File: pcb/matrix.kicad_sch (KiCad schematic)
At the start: 179 parts, among them SW10 Tab, SW11 CapsLock, SW12 Shift, SW13 Ctrl, SW14 F1, SW15 1, SW16 Q, SW17 A, SW18 Z, SW19 Win, SW20 F2, SW21 2, SW22 W, SW23 S, SW24 X, SW25 F3, SW26 3, SW27 E, SW28 D, SW29 C, SW30 F4, SW31 4, SW32 R, SW33 F, SW34 V, SW35 F5, SW36 5, SW37 T, SW38 G, SW39 B, SW4 M1, SW40 Space, SW41 F6, SW42 6, SW43 Y, SW44 H, SW45 N, SW46 F7, SW47 7, SW48 U, SW49 J, SW5 M2, SW50 M, SW51 F8, SW52 8, SW53 I, SW54 K, SW55 Comma, SW56 RAlt, SW57 F9, SW58 9, SW59 O, SW6 M3, SW60 L, SW61 Period, SW62 RFn, SW63 F10, SW64 0, SW65 P, SW66 Semicolon, SW67 Slash, SW68 RCtrl, SW69 F11, SW7 M4, SW70 Minus, SW71 LBrkt, SW72 Quote, SW73 RShift, SW74 F12, SW75 Equals, SW76 RBrkt, SW77 Enter, SW78 LArr, SW79 F13, SW8 Esc, SW80 Bksp, SW81 Bkslash, SW82 UArr, SW83 DArr, SW84 Knob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

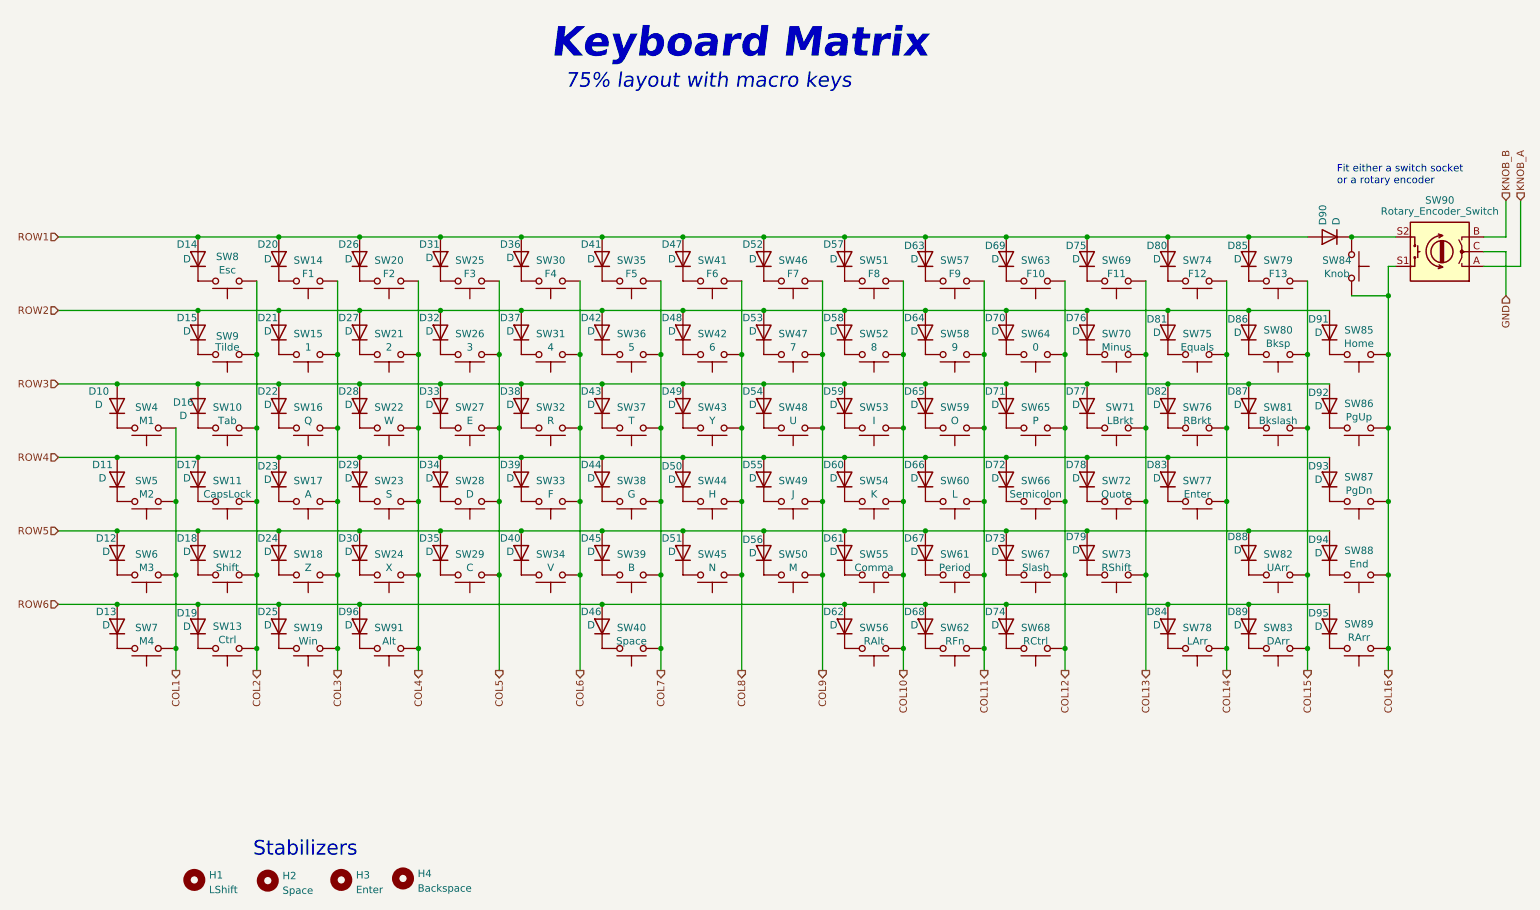
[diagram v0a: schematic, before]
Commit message: Change value fields for socket assembly
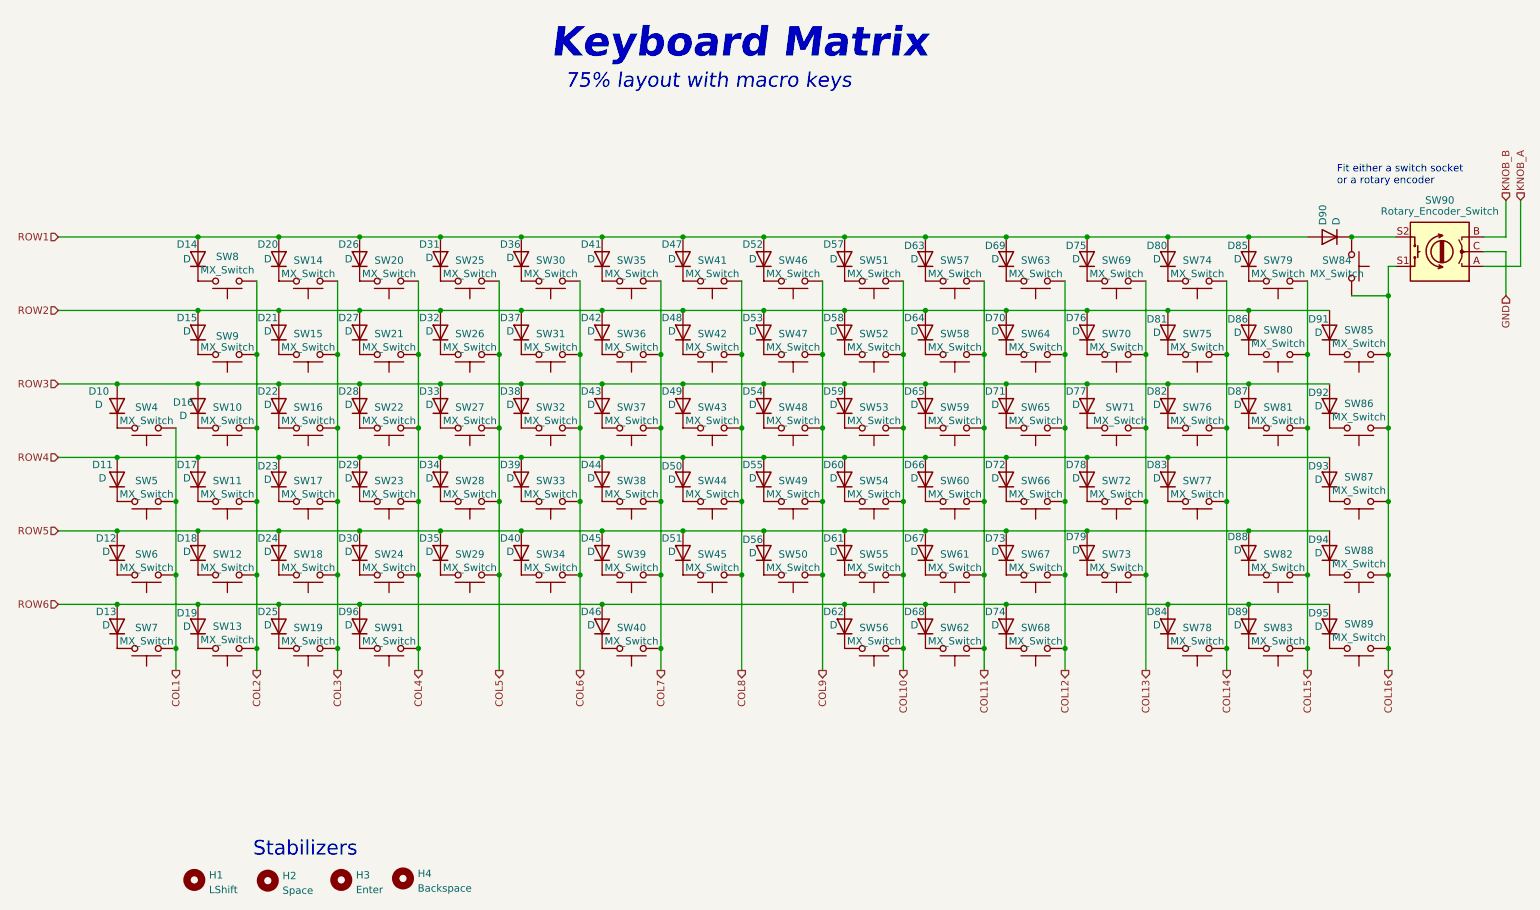
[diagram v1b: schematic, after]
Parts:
- SW10: value Tab -> MX_Switch; LSCS (none) -> C5156480
- SW11: value CapsLock -> MX_Switch; LSCS (none) -> C5156480
- SW12: value Shift -> MX_Switch; LSCS (none) -> C5156480
- SW13: value Ctrl -> MX_Switch; LSCS (none) -> C5156480
- SW14: value F1 -> MX_Switch; LSCS (none) -> C5156480
- SW15: value 1 -> MX_Switch; LSCS (none) -> C5156480
- SW16: value Q -> MX_Switch; LSCS (none) -> C5156480
- SW17: value A -> MX_Switch; LSCS (none) -> C5156480
- SW18: value Z -> MX_Switch; LSCS (none) -> C5156480
- SW19: value Win -> MX_Switch; LSCS (none) -> C5156480
- SW20: value F2 -> MX_Switch; LSCS (none) -> C5156480
- SW21: value 2 -> MX_Switch; LSCS (none) -> C5156480
- SW22: value W -> MX_Switch; LSCS (none) -> C5156480
- SW23: value S -> MX_Switch; LSCS (none) -> C5156480
- SW24: value X -> MX_Switch; LSCS (none) -> C5156480
- SW25: value F3 -> MX_Switch; LSCS (none) -> C5156480
- SW26: value 3 -> MX_Switch; LSCS (none) -> C5156480
- SW27: value E -> MX_Switch; LSCS (none) -> C5156480
- SW28: value D -> MX_Switch; LSCS (none) -> C5156480
- SW29: value C -> MX_Switch; LSCS (none) -> C5156480
- SW30: value F4 -> MX_Switch; LSCS (none) -> C5156480
- SW31: value 4 -> MX_Switch; LSCS (none) -> C5156480
- SW32: value R -> MX_Switch; LSCS (none) -> C5156480
- SW33: value F -> MX_Switch; LSCS (none) -> C5156480
- SW34: value V -> MX_Switch; LSCS (none) -> C5156480
- SW35: value F5 -> MX_Switch; LSCS (none) -> C5156480
- SW36: value 5 -> MX_Switch; LSCS (none) -> C5156480
- SW37: value T -> MX_Switch; LSCS (none) -> C5156480
- SW38: value G -> MX_Switch; LSCS (none) -> C5156480
- SW39: value B -> MX_Switch; LSCS (none) -> C5156480
- SW4: value M1 -> MX_Switch; LSCS (none) -> C5156480
- SW40: value Space -> MX_Switch; LSCS (none) -> C5156480
- SW41: value F6 -> MX_Switch; LSCS (none) -> C5156480
- SW42: value 6 -> MX_Switch; LSCS (none) -> C5156480
- SW43: value Y -> MX_Switch; LSCS (none) -> C5156480
- SW44: value H -> MX_Switch; LSCS (none) -> C5156480
- SW45: value N -> MX_Switch; LSCS (none) -> C5156480
- SW46: value F7 -> MX_Switch; LSCS (none) -> C5156480
- SW47: value 7 -> MX_Switch; LSCS (none) -> C5156480
- SW48: value U -> MX_Switch; LSCS (none) -> C5156480
- SW49: value J -> MX_Switch; LSCS (none) -> C5156480
- SW5: value M2 -> MX_Switch; LSCS (none) -> C5156480
- SW50: value M -> MX_Switch; LSCS (none) -> C5156480
- SW51: value F8 -> MX_Switch; LSCS (none) -> C5156480
- SW52: value 8 -> MX_Switch; LSCS (none) -> C5156480
- SW53: value I -> MX_Switch; LSCS (none) -> C5156480
- SW54: value K -> MX_Switch; LSCS (none) -> C5156480
- SW55: value Comma -> MX_Switch; LSCS (none) -> C5156480
- SW56: value RAlt -> MX_Switch; LSCS (none) -> C5156480
- SW57: value F9 -> MX_Switch; LSCS (none) -> C5156480
- SW58: value 9 -> MX_Switch; LSCS (none) -> C5156480
- SW59: value O -> MX_Switch; LSCS (none) -> C5156480
- SW6: value M3 -> MX_Switch; LSCS (none) -> C5156480
- SW60: value L -> MX_Switch; LSCS (none) -> C5156480
- SW61: value Period -> MX_Switch; LSCS (none) -> C5156480
- SW62: value RFn -> MX_Switch; LSCS (none) -> C5156480
- SW63: value F10 -> MX_Switch; LSCS (none) -> C5156480
- SW64: value 0 -> MX_Switch; LSCS (none) -> C5156480
- SW65: value P -> MX_Switch; LSCS (none) -> C5156480
- SW66: value Semicolon -> MX_Switch; LSCS (none) -> C5156480
- SW67: value Slash -> MX_Switch; LSCS (none) -> C5156480
- SW68: value RCtrl -> MX_Switch; LSCS (none) -> C5156480
- SW69: value F11 -> MX_Switch; LSCS (none) -> C5156480
- SW7: value M4 -> MX_Switch; LSCS (none) -> C5156480
- SW70: value Minus -> MX_Switch; LSCS (none) -> C5156480
- SW71: value LBrkt -> MX_Switch; LSCS (none) -> C5156480
- SW72: value Quote -> MX_Switch; LSCS (none) -> C5156480
- SW73: value RShift -> MX_Switch; LSCS (none) -> C5156480
- SW74: value F12 -> MX_Switch; LSCS (none) -> C5156480
- SW75: value Equals -> MX_Switch; LSCS (none) -> C5156480
- SW76: value RBrkt -> MX_Switch; LSCS (none) -> C5156480
- SW77: value Enter -> MX_Switch; LSCS (none) -> C5156480
- SW78: value LArr -> MX_Switch; LSCS (none) -> C5156480
- SW79: value F13 -> MX_Switch; LSCS (none) -> C5156480
- SW8: value Esc -> MX_Switch; LSCS (none) -> C5156480
- SW80: value Bksp -> MX_Switch; LSCS (none) -> C5156480
- SW81: value Bkslash -> MX_Switch; LSCS (none) -> C5156480
- SW82: value UArr -> MX_Switch; LSCS (none) -> C5156480
- SW83: value DArr -> MX_Switch; LSCS (none) -> C5156480
- SW84: value Knob -> MX_Switch; LSCS (none) -> C5156480
- SW85: value Home -> MX_Switch; LSCS (none) -> C5156480
- SW86: value PgUp -> MX_Switch; LSCS (none) -> C5156480
- SW87: value PgDn -> MX_Switch; LSCS (none) -> C5156480
- SW88: value End -> MX_Switch; LSCS (none) -> C5156480
- SW89: value RArr -> MX_Switch; LSCS (none) -> C5156480
- SW9: value Tilde -> MX_Switch; LSCS (none) -> C5156480
- SW91: value Alt -> MX_Switch; LSCS (none) -> C5156480

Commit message: Move SWD header, fix DRC issues
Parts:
- SW84: footprint Switch_Keyboard_Kailh:SW_Hotswap_Kailh_MX_plated_1.00u -> Switch_Keyboard_Kailh:SW_Hotswap_Kailh_MX_1.00u
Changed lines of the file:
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@@
     (property "Reference" "SW84" (id 0) (at 247.65 72.6186 90))
     (property "Value" "MX_Switch" (id 1) (at 247.65 74.93 90))
-    (property "Footprint" "Switch_Keyboard_Kailh:SW_Hotswap_Kailh_MX_plated_1.00u" (id 2) (at 255.27 73.66 0)
+    (property "Footprint" "Switch_Keyboard_Kailh:SW_Hotswap_Kailh_MX_1.00u" (id 2) (at 255.27 73.66 0)
       (effects (font (size 1.27 1.27)) hide)
     )

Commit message: Add solder bridge for power led, add silkscreen for pin headers
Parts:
- H1, H3, H4: footprint Mounting_Keyboard_Stabilizer:Stabilizer_Cherry_MX_2u -> Mounting_Keyboard_Stabilizer:Stabilizer_Cherry_MX_2.00u
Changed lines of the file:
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@@
       (effects (font (size 1.27 1.27)) (justify left))
     )
-    (property "Footprint" "Mounting_Keyboard_Stabilizer:Stabilizer_Cherry_MX_2u" (id 2) (at 50.165 179.705 0)
+    (property "Footprint" "Mounting_Keyboard_Stabilizer:Stabilizer_Cherry_MX_2.00u" (id 2) (at 50.165 179.705 0)
       (effects (font (size 1.27 1.27)) hide)
     )
@@
       (effects (font (size 1.27 1.27)) (justify left))
     )
-    (property "Footprint" "Mounting_Keyboard_Stabilizer:Stabilizer_Cherry_MX_2u" (id 2) (at 75.565 179.705 0)
+    (property "Footprint" "Mounting_Keyboard_Stabilizer:Stabilizer_Cherry_MX_2.00u" (id 2) (at 75.565 179.705 0)
       (effects (font (size 1.27 1.27)) hide)
     )
@@
       (effects (font (size 1.27 1.27)) (justify left))
     )
-    (property "Footprint" "Mounting_Keyboard_Stabilizer:Stabilizer_Cherry_MX_2u" (id 2) (at 86.233 179.451 0)
-      (effects (font (size 1.27 1.27)) hide)
-    )
+    (property "Footprint" "Mounting_Keyboard_Stabilizer:Stabilizer_Cherry_MX_2.00u" (id 2) (at 86.233 179.451 0)
+      (effects (font (size 1.27 1.27)) hide)
+    )
